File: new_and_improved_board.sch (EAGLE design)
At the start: 23 parts, among them J4 455-1750-1-ND, Q2 IRF3704L-V

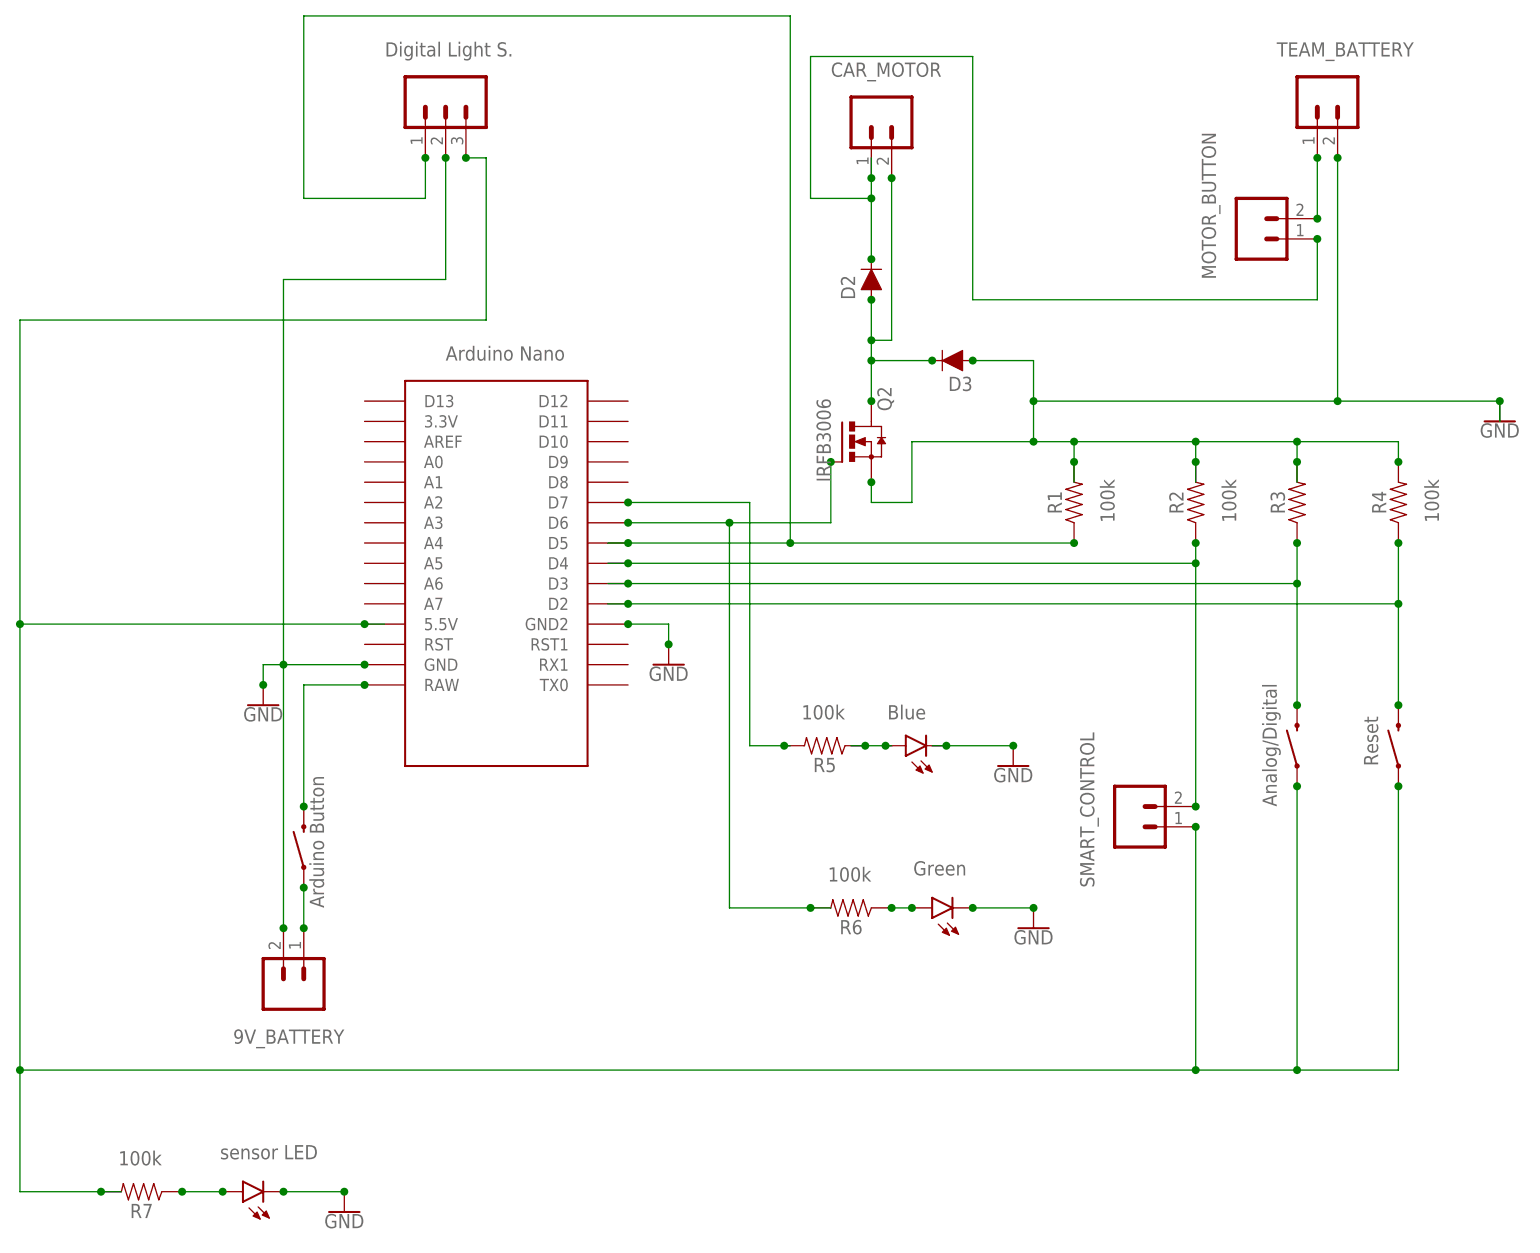
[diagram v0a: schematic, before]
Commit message: added ground and power planes, and changed resistor values/added resistor after the mosfet gate
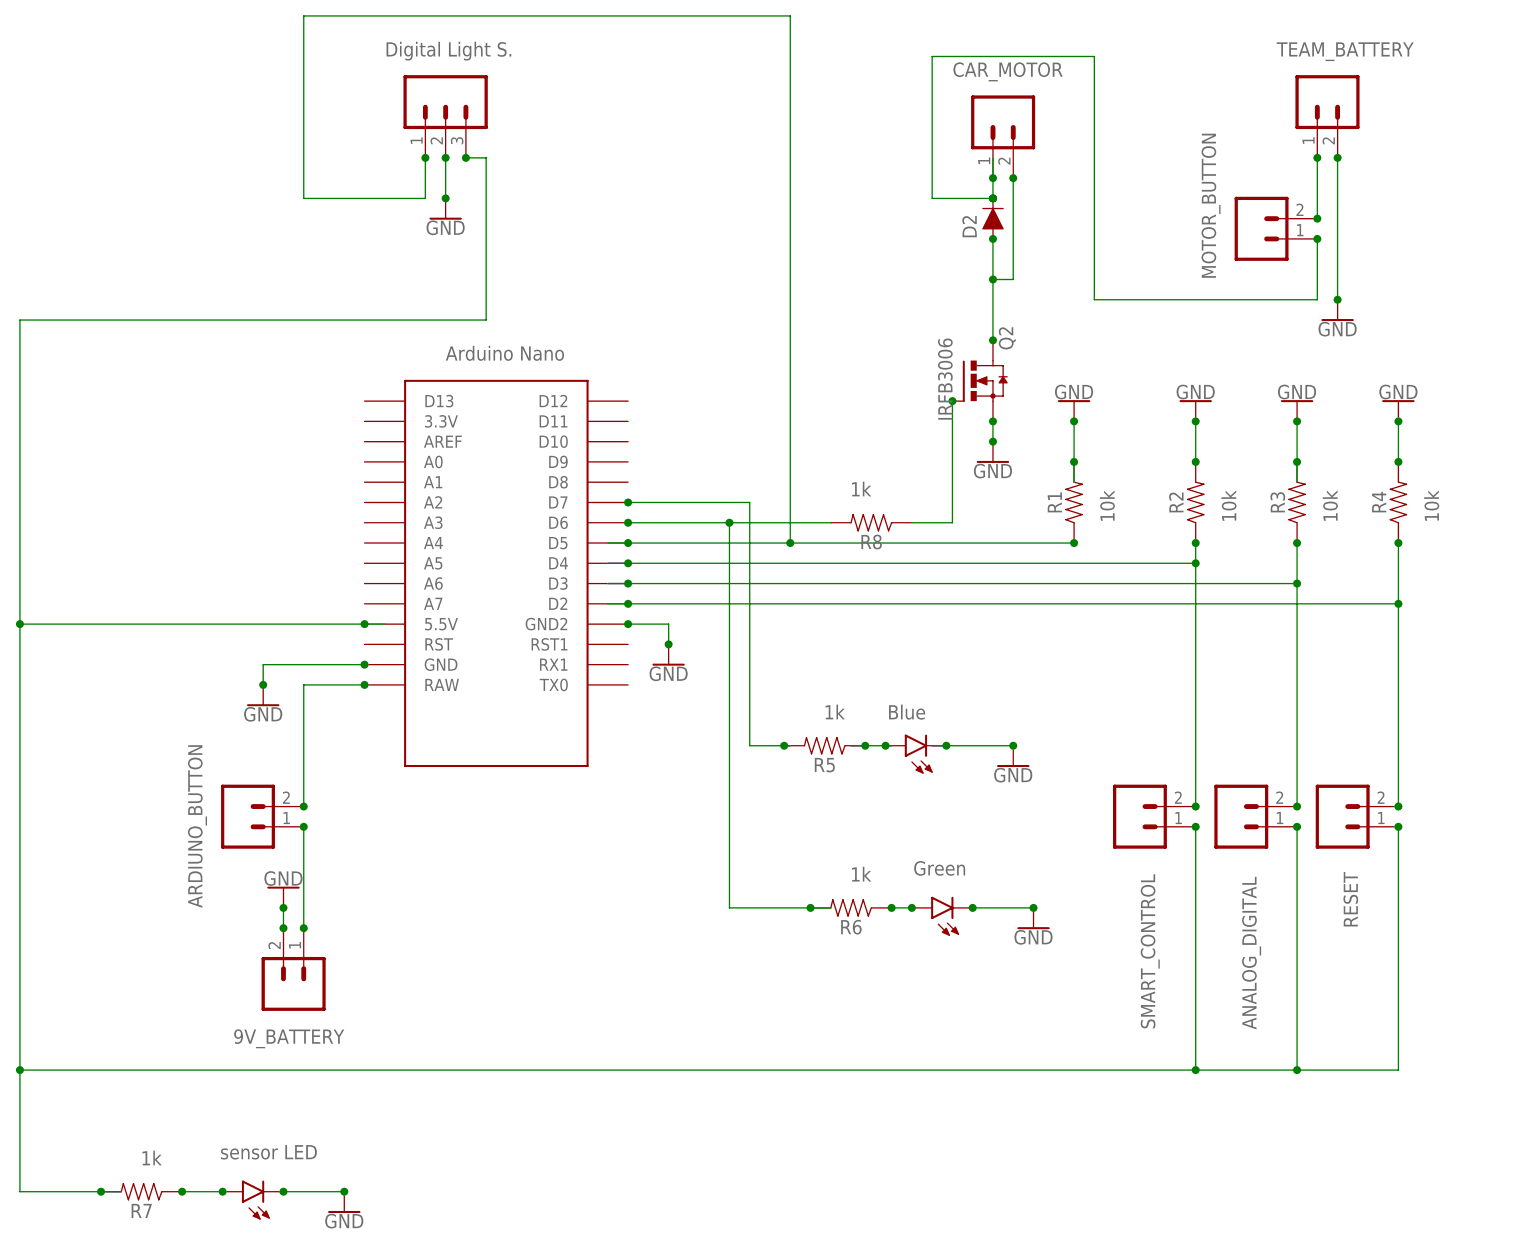
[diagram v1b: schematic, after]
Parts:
- removed D3: 200mA/100V/1V, SparkFun-DiscreteSemi:DIODE-1N4148
- added R8: 1M, SparkFun-Resistors:1MOHM-HORIZ-1/6W-5%
- R1, R2, R4: PROD_ID 100k -> 10k
- R3: PROD_ID (none) -> 10k
- R5, R6, R7: PROD_ID 100k -> 1k
- S1: value MOMENTARY-SWITCH-SPST-SMD-RIGHT-ANGLE -> (none); device SparkFun-Switches:MOMENTARY-SWITCH-SPST-SMD-RIGHT-ANGLE -> SparkFun-Connectors:CONN_02; PROD_ID Arduino Button -> (none)
- S4: value MOMENTARY-SWITCH-SPST-SMD-RIGHT-ANGLE -> (none); device SparkFun-Switches:MOMENTARY-SWITCH-SPST-SMD-RIGHT-ANGLE -> SparkFun-Connectors:CONN_02; PROD_ID Analog/Digital -> (none)
- S5: value MOMENTARY-SWITCH-SPST-SMD-RIGHT-ANGLE -> (none); device SparkFun-Switches:MOMENTARY-SWITCH-SPST-SMD-RIGHT-ANGLE -> SparkFun-Connectors:CONN_02; PROD_ID Reset -> (none)
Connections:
- net N$12 renamed 9VBAT
- net N$13 renamed 9V
- net N$16 renamed 5V
- net GND: now also J3.2, Q2.S, R1.2, R2.2, R3.2, R4.2
- net N$1: now also R8.2; no longer Q2.G
- net N$2: no longer D3.C
- net N$3: now also Q2.G, R8.1; no longer D3.A, J3.2, Q2.S, R1.2, R2.2, R3.2, R4.2
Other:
- moved on the sheet: D2, Q2
